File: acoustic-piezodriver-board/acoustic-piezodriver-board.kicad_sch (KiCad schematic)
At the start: 6 parts, among them P101 WJ128V-5.0-3P, U101 AMS1117-3.3, U102 TMCS1108A3UQDR

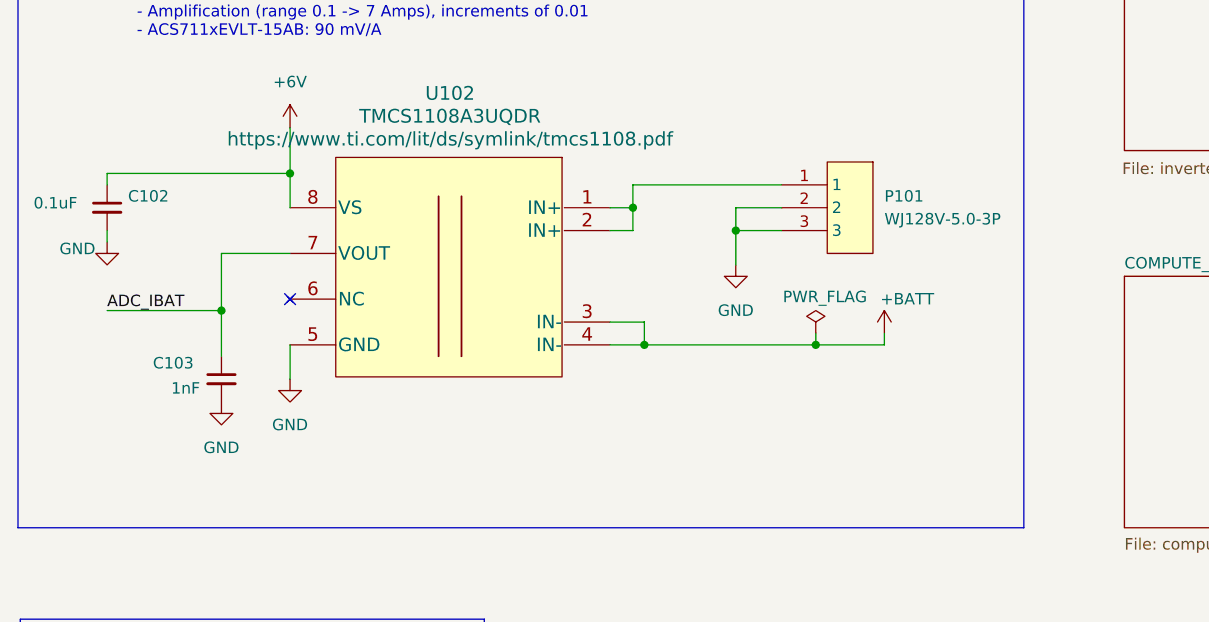
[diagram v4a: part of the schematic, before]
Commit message: replaced dual 10uH inductors with single 22uH higher VDC resistant one, started laying out 40 V boost
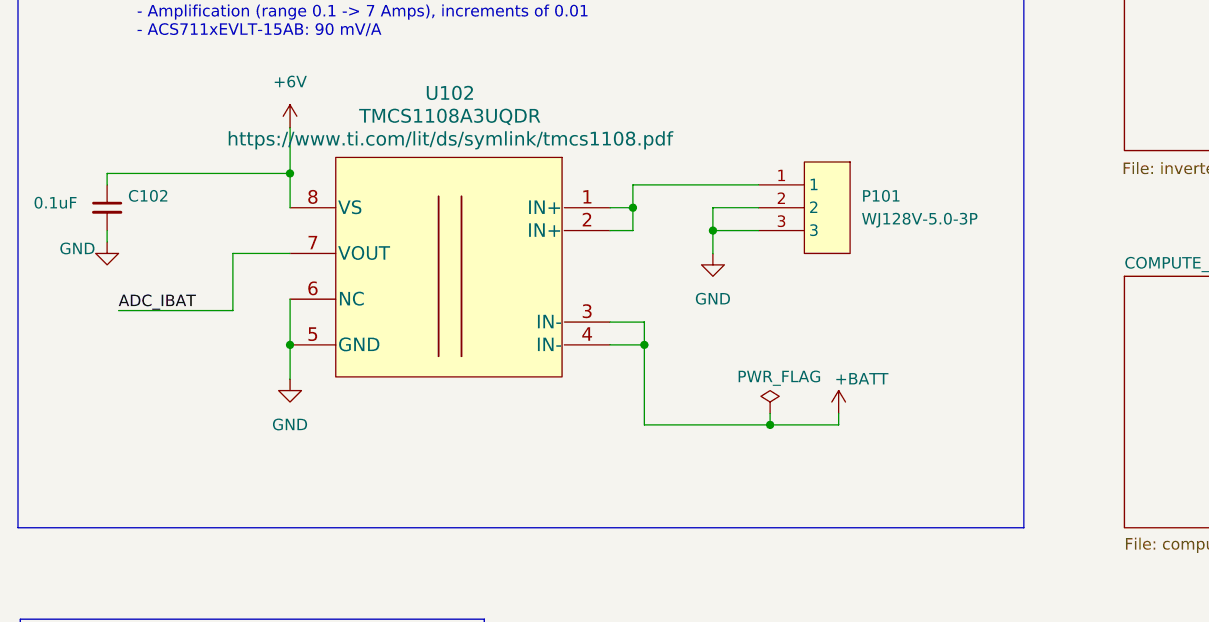
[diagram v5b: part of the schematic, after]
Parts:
- removed C103: 1nF, Capacitor_SMD:C_0402_1005Metric, symbol Device:C_Small
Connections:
- net GND: now also U102.6 (NC)
- no-connect marks 1 -> 0
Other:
- moved on the sheet: P101
